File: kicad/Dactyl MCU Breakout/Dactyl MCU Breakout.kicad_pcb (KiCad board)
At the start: 2 copper layers, 53.9 x 61.6 mm, 44 parts, among them J1 Columns, J2 Rows, J3 Thumbs, J5 Display, J6 External, J7 JST, J8 Split, J9 Vic, K1 Key, SW1 Battery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

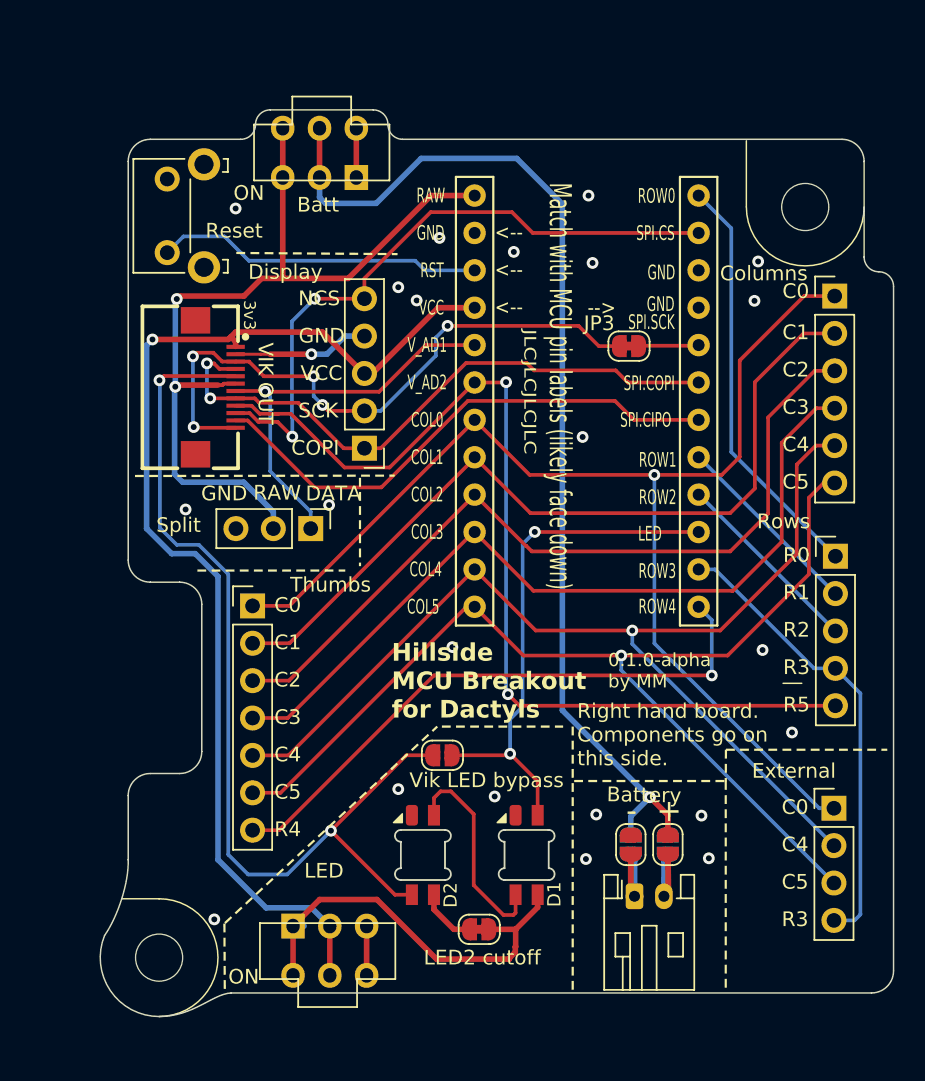
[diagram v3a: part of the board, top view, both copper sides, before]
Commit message: feat: split USB-C
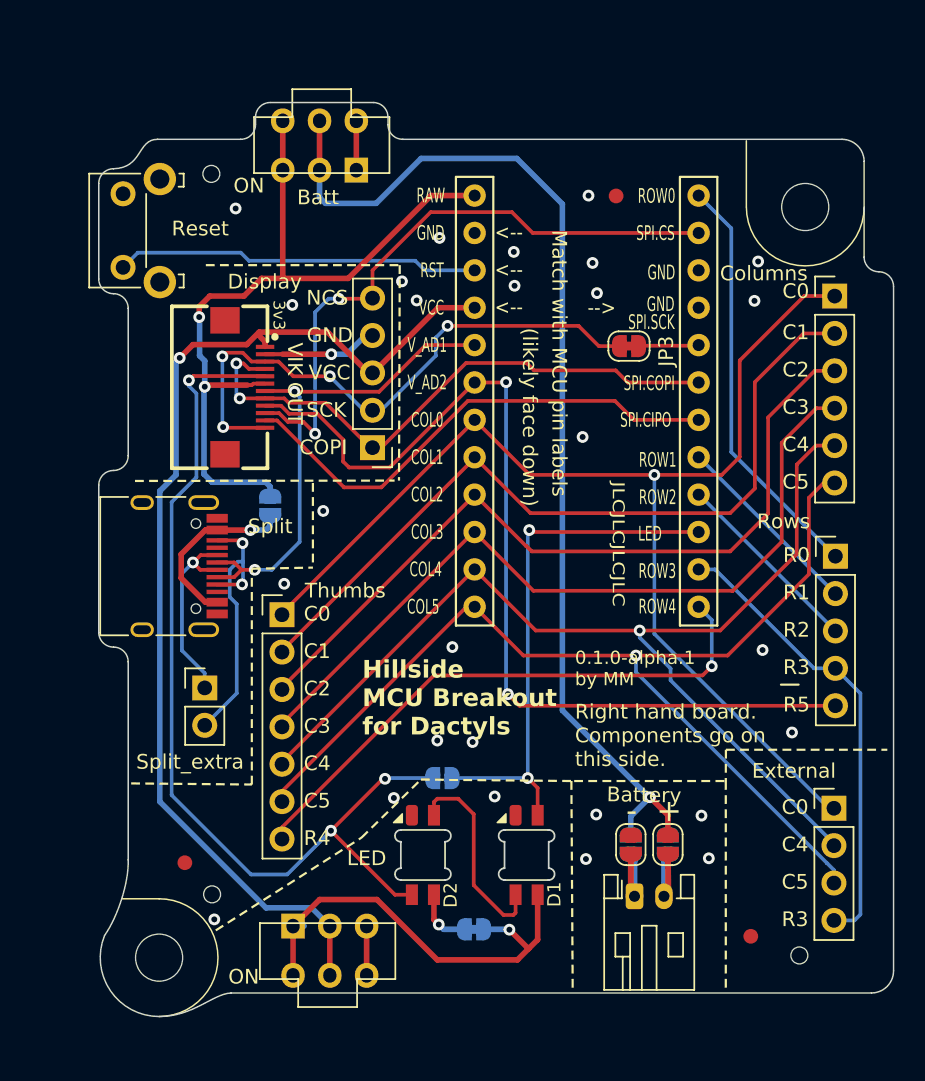
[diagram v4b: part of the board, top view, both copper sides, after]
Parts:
- added FID1: Fiducial, Fiducial:Fiducial_1mm_Mask2mm, F.Cu at (133.2, 53.9)
- added FID2: Fiducial, Fiducial:Fiducial_1mm_Mask2mm, F.Cu at (103.8, 99.2)
- added FID3: Fiducial, Fiducial:Fiducial_1mm_Mask2mm, F.Cu at (142.3, 104.2)
- added H3: ToolingHole, Dactyl:ToolingHole_1.152mm, F.Cu at (105.7, 52.4)
- added H4: ToolingHole, Dactyl:ToolingHole_1.152mm, F.Cu at (105.7, 101.3)
- added H5: ToolingHole, Dactyl:ToolingHole_1.152mm, F.Cu at (145.6, 105.5)
- added J4: Split, Connector_USB:USB_C_Receptacle_HRO_TYPE-C-31-M-12, F.Cu at (102.0, 79.0)
- added JP4: Split power, Jumper:SolderJumper-2_P1.3mm_Open_RoundedPad1.0x1.5mm, B.Cu at (109.7, 74.9)
- J8: value Split -> Split_extra; footprint Connector_PinHeader_2.54mm:PinHeader_1x03_P2.54mm_Vertical -> Connector_PinHeader_2.54mm:PinHeader_1x02_P2.54mm_Vertical
- JP1: value LED2 cutoff -> LED2 power; moved to B.Cu
- JP2: moved to B.Cu
- U1: footprint Dactyl:ProMicro_v2_1 -> Dactyl:ProMicro_v2_1S
- moved J8 13.0 mm to (105.2, 87.3), turned to 0 degrees
- moved K1 8.85 mm to (71.3, 132.7)
- moved K1 8.85 mm to (89.3, 132.7)
- moved K1 8.85 mm to (71.3, 149.8)
- moved K1 8.85 mm to (107.3, 149.9)
- moved K1 8.85 mm to (89.3, 149.8)
- moved SW2 3.16 mm to (100.9, 56.2)
- moved J3 2.09 mm to (110.5, 82.3)
- moved J9 2.00 mm to (107.3, 66.8)
- moved JP2 1.55 mm to (121.3, 93.4)
- moved J5 0.55 mm to (116.6, 71.0)
- moved SW1 0.50 mm to (113.0, 50.4)
- moved JP1 0.35 mm to (123.5, 103.7)
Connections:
- J8 pad 1: /Right/SPLIT_VIK_GP_AD1 -> Net-(J8-Pin_1)
- J8 pad 2: /Right/RAW -> Net-(J4-SBU1)
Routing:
- net Net-(J4-SBU1): track 0.00 -> 19.1 mm, vias 0 -> 2
- net Net-(J8-Pin_1): track 0.00 -> 13.2 mm, vias 0 -> 1
- net /Right/split_RAW: track 0.00 -> 12.3 mm, vias 0 -> 1
- net /Right/SPLIT_VIK_GP_AD1: track 28.2 -> 34.4 mm, vias 1 -> 2
- net /Right/RAW: track 55.1 -> 50.4 mm
- net /Right/VCC: track 73.8 -> 70.3 mm
- net /Right/SPI0.SCK/SDA: track 42.9 -> 40.1 mm, vias 5 -> 4
- net /Right/RST: track 22.3 -> 24.8 mm
- net /Right/VCC_LED1: track 24.1 -> 26.3 mm, vias 0 -> 1
- net /Right/col0: track 83.5 -> 81.4 mm
- net /Right/SPI0.COPI/SCL: track 42.1 -> 40.1 mm
- net /Right/SPI0.CIPO: track 36.3 -> 34.3 mm
- net /Right/col4: track 75.6 -> 73.7 mm
- net /Right/col5: track 75.5 -> 73.7 mm
- net /Right/col1: track 55.7 -> 54.0 mm
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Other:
- board size 53.9 x 61.6 mm -> 54 x 62.1 mm
- board text added: "(likely face down)"
- board text added: "Match with MCU pin labels"
- board text removed: "TRRS fits in split area"

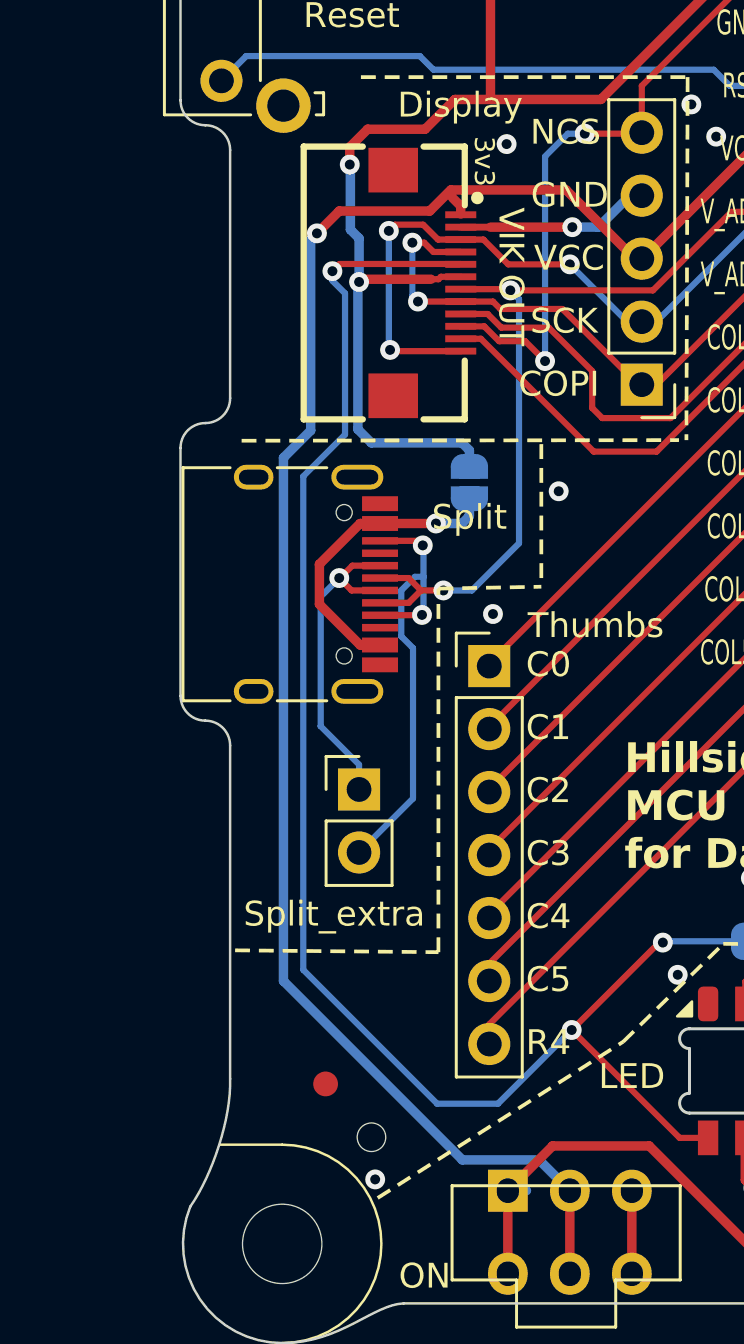
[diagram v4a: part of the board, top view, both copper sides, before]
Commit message: feat: split usb sticks out more
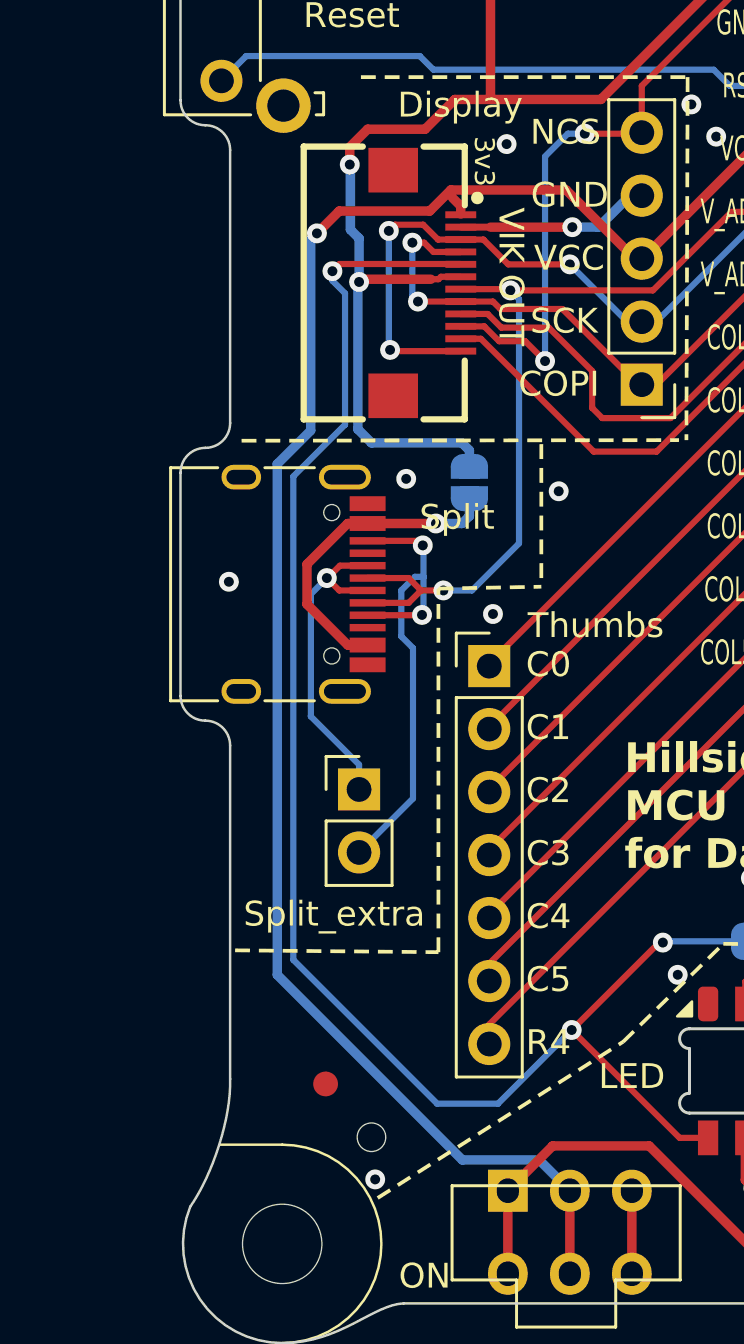
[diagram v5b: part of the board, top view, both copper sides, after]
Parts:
- moved J4 0.50 mm to (101.5, 79.0)
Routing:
- net Net-(J4-SBU1): track 19.1 -> 20.1 mm
- net /Right/SPLIT_VIK_GP_AD1: track 34.4 -> 35.4 mm
- net /Right/split_RAW: track 12.3 -> 12.8 mm
- net GND: vias 28 -> 30
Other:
- outline, holes or cut-outs redrawn

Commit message: feat(PCB): get rid of example keys
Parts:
- removed K1 (x25): Key, Dactyl:pg1350

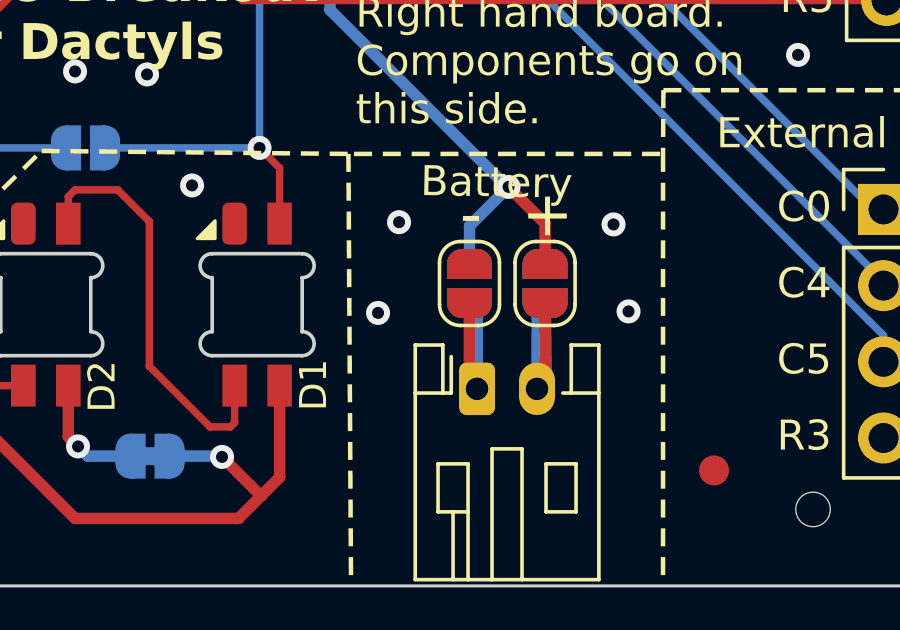
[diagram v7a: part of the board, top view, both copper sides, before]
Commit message: doc: schema doc cleanup
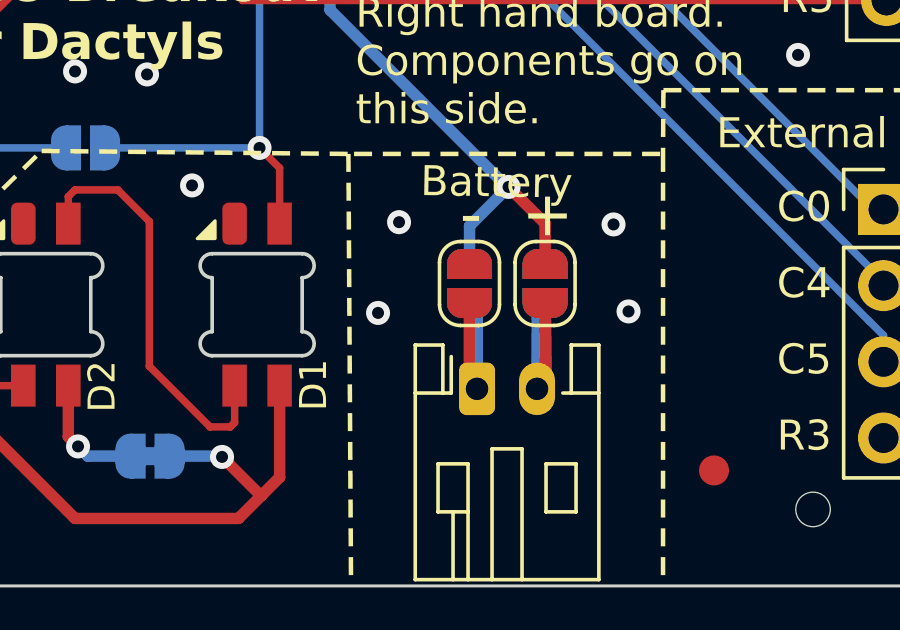
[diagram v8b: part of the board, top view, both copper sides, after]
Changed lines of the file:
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@@
 		(fp_arc
 			(start 6.938123 15.132041)
-			(mid 6.337066 14.8831)
+			(mid 6.337062 14.8831)
 			(end 6.088123 14.282041)
 			(stroke
@@
 		(fp_arc
 			(start 8.236041 -15.740877)
-			(mid 8.837089 -15.491924)
+			(mid 8.837086 -15.491923)
 			(end 9.086041 -14.890877)
 			(stroke
@@
 		(fp_arc
 			(start 1.550062 2.100001)
-			(mid 2.045036 2.305028)
+			(mid 2.045039 2.305027)
 			(end 2.250063 2.800003)
 			(stroke
@@
 		(fp_arc
 			(start 1.551371 2.100001)
-			(mid 2.046344 2.305026)
+			(mid 2.046348 2.305026)
 			(end 2.251372 2.8)
 			(stroke
